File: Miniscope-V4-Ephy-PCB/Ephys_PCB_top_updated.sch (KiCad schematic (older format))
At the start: 41 parts, among them J1 34 Circuit Slimslack Connector, J10 Conn_01x01, J11 Conn_01x01, J12 Conn_01x01, J13 Conn_01x01, J4 Conn_01x01, J5 Conn_01x01, J8 Conn_01x01, U1 ATSAMS70N21A-CFNT, U2 RHD2132_QFN-RHD2132, U3 ABM8G-12.000MHZ-4Y-T3, U4 TXB0304RUT, U5 LTST-C191KRKT, U6 TLV7103318DSER

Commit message: Update schematic and footprints
* Replaced MCU symbol, pinout, and footprint with correct one (TFBGA version).
* Created and replaced slimstack connector with the correct one.
* Replaced crystal oscillator with better symbol
* Tried to link as many footprints as possible to those contained in the Aharoni KiCad Library.
* TODO: Add transistor to drive status LED.
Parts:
- removed C1, C3: GRM155R60J475ME87D, cap_GRM155R60J475ME47D:GRM155R60J475ME47D, symbol .Capacitor:GRM155R60J475ME87D
- removed U1: ATSAMS70N21A-CFNT, ATSAMS70N21ACFNT:ATSAMS70N21A-CFNT, symbol Ephys_PCB_top_updated-rescue:ATSAMS70N21A-CFNT-ATSAMS7-N21
- removed U3: ABM8G-12.000MHZ-4Y-T3, ABM8G-12:OSCSC320X250X100N, symbol Ephys_PCB_top_updated-rescue:ABM8G-12.000MHZ-4Y-T3-ABM8G-12.000MHZ-4Y-T3
- removed U6: TLV7103318DSER, TLV7103318DSER_ldo:TLV7103318DSER, symbol .Regulator_Linear:TLV7103318DSER
- added C1, C3: 4.7uF, .Capacitor:C_0402_1005Metric_L, symbol .Device:C_Small
- added U1: ATSAME70N21A-CN, .Package_BGA:BGA_100_CP80_10X10_900X900X110B40L, symbol .MCU:ATSAME70N21A-CN
- added U3: TLV7103318DSER, .Package_SON:SON_6_P50_150X150X80L50X25L, symbol .Regulator_Linear:TLV7103318DSER
- added Y1: ABM8G-12.000MHZ-4Y-T3, .Oscillator:OSCCC320X250X100L80X100, symbol .Oscillator:ABM8G-12.000MHZ-4Y-T3
- J1: footprint Connector_Molex:Molex_SlimStack_55560-0341_2x17_P0.50mm_Vertical -> .Connector:SS_5046223412
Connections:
- net labels added: VDDUTMIC
- net labels removed: LINEVALID, SPI1_NPCS0, VDDMIC
- wire segments 246 -> 235
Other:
- note removed: "Should have overlapping pins (pins 2 and 4) in the schematic"
- note removed: "You had 1.8V connected to VDDOUT which I don't think is correct."
- moved on the sheet: C17, C18, R1, R3, R4

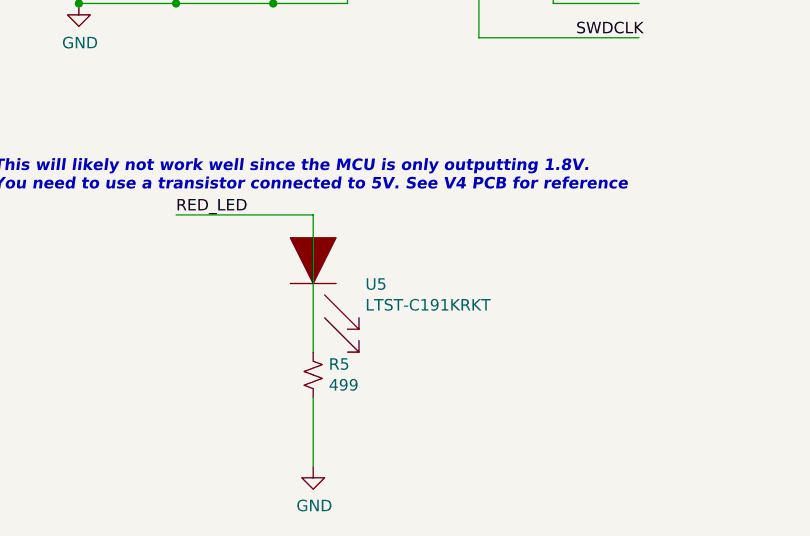
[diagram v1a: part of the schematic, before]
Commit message: Group components in PCB layout
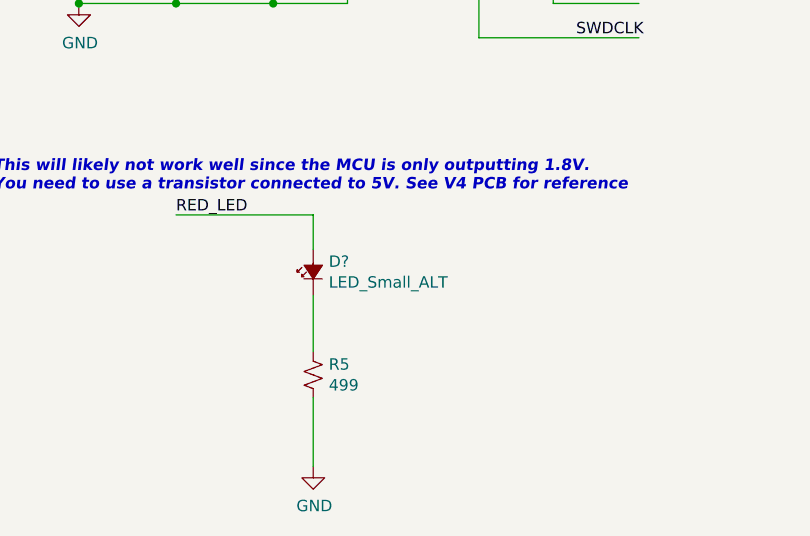
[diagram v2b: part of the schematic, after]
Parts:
- removed U5: LTST-C191KRKT, LED_SMD:LED_0402_1005Metric, symbol .LED:LTST-C191KRKT
- added D?: LED_Small_ALT, LED_SMD:LED_0402_1005Metric, symbol .Device:LED_Small_ALT
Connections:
- wire segments 235 -> 236
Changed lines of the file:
@@
 $EndComp
-$Comp
-L .LED:LTST-C191KRKT U5
-U 1 1 5F09DD3F
-P 10150 9875
-F 0 "U5" V 10204 10103 50  0000 L CNN
-F 1 "LTST-C191KRKT" V 10295 10103 50  0000 L CNN
-F 2 "LED_SMD:LED_0402_1005Metric" H 10150 9875 50  0001 C CNN
-F 3 "" H 10150 9875 50  0001 C CNN
-	1    10150 9875
-	0    1    1    0
-$EndComp
-Wire Wire Line
-	10150 9625 10150 10225
 $Comp
 L power:GND #PWR0128
@@
 	0    1    1    0
 $EndComp
+$Comp
+L .Device:LED_Small_ALT D?
+U 1 1 5F58077D
+P 10150 9875
+F 0 "D?" V 10196 9807 50  0000 R CNN
+F 1 "LED_Small_ALT" V 10105 9807 50  0000 R CNN
+F 2 "LED_SMD:LED_0402_1005Metric" V 10150 9875 50  0001 C CNN
+F 3 "~" V 10150 9875 50  0001 C CNN
+	1    10150 9875
+	0    -1   -1   0
+$EndComp
+Wire Wire Line
+	10150 9625 10150 9775
+Wire Wire Line
+	10150 9975 10150 10225
 $EndSCHEMATC

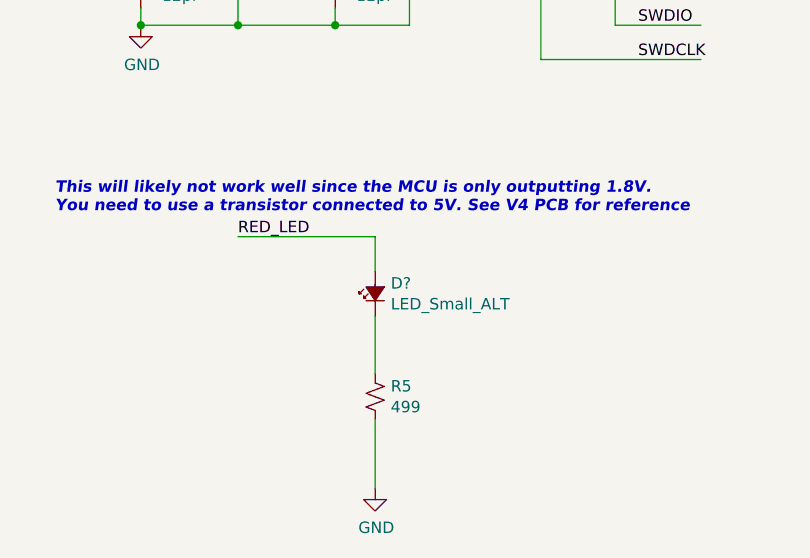
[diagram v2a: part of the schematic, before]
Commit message: Update Board Setup Specifications
Via: 0.15mm/0,3mm
Trace/Space: 3mil/3mil
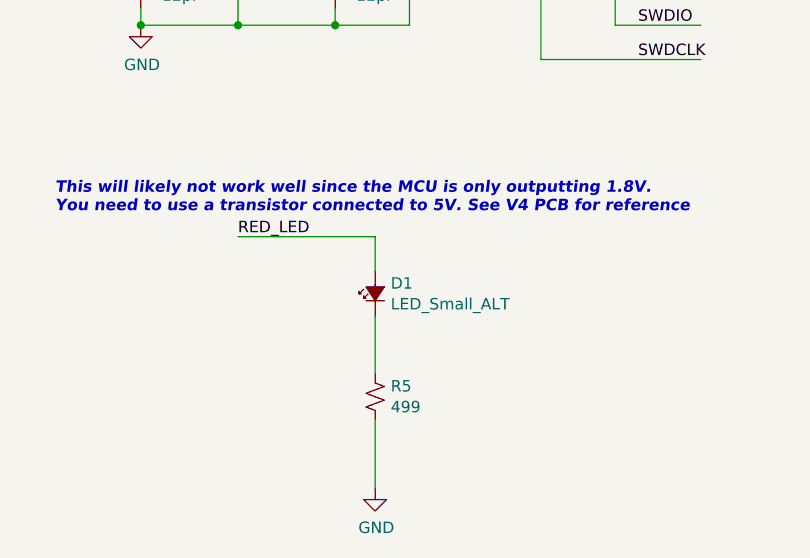
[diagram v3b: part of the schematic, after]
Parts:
- gave numbers to parts that had none: 1
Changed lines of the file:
@@
 $EndComp
 $Comp
-L .Device:LED_Small_ALT D?
+L .Device:LED_Small_ALT D1
 U 1 1 5F58077D
 P 10150 9875
-F 0 "D?" V 10196 9807 50  0000 R CNN
+F 0 "D1" V 10196 9807 50  0000 R CNN
 F 1 "LED_Small_ALT" V 10105 9807 50  0000 R CNN
 F 2 "LED_SMD:LED_0402_1005Metric" V 10150 9875 50  0001 C CNN

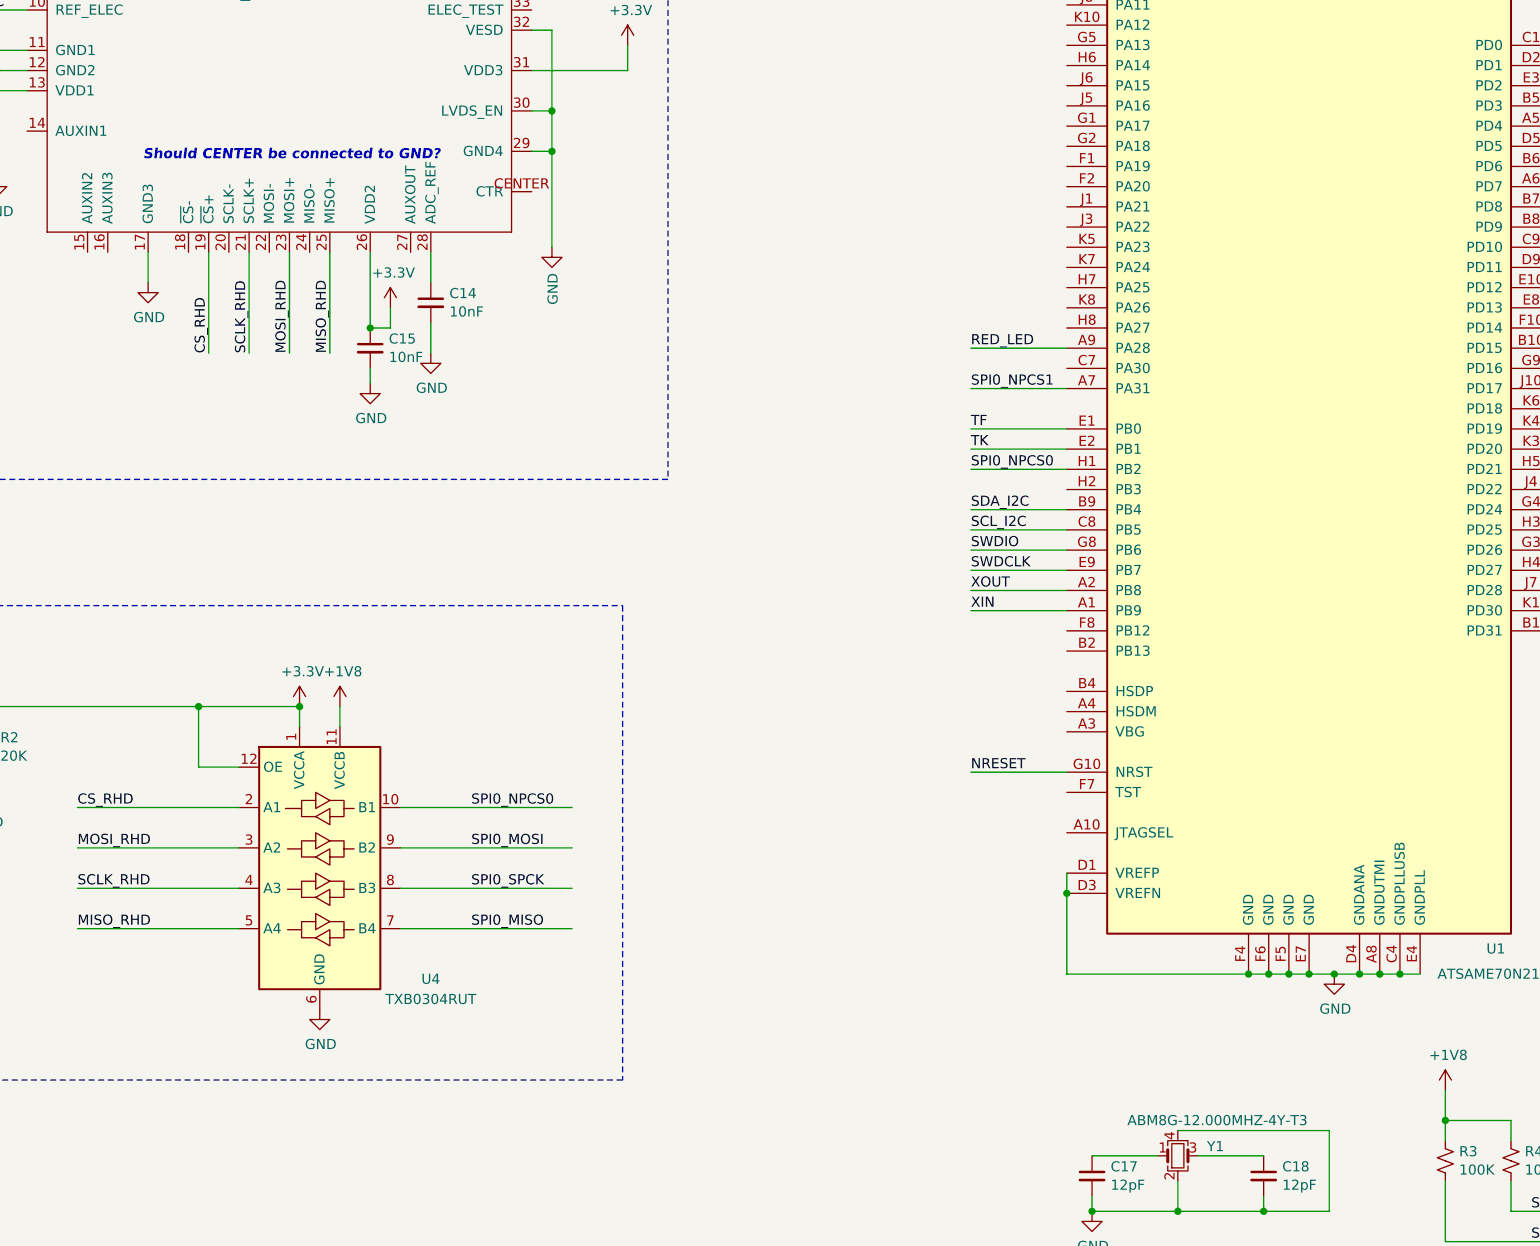
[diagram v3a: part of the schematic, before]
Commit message: Move things around in PCBnew and add prelim board outline.
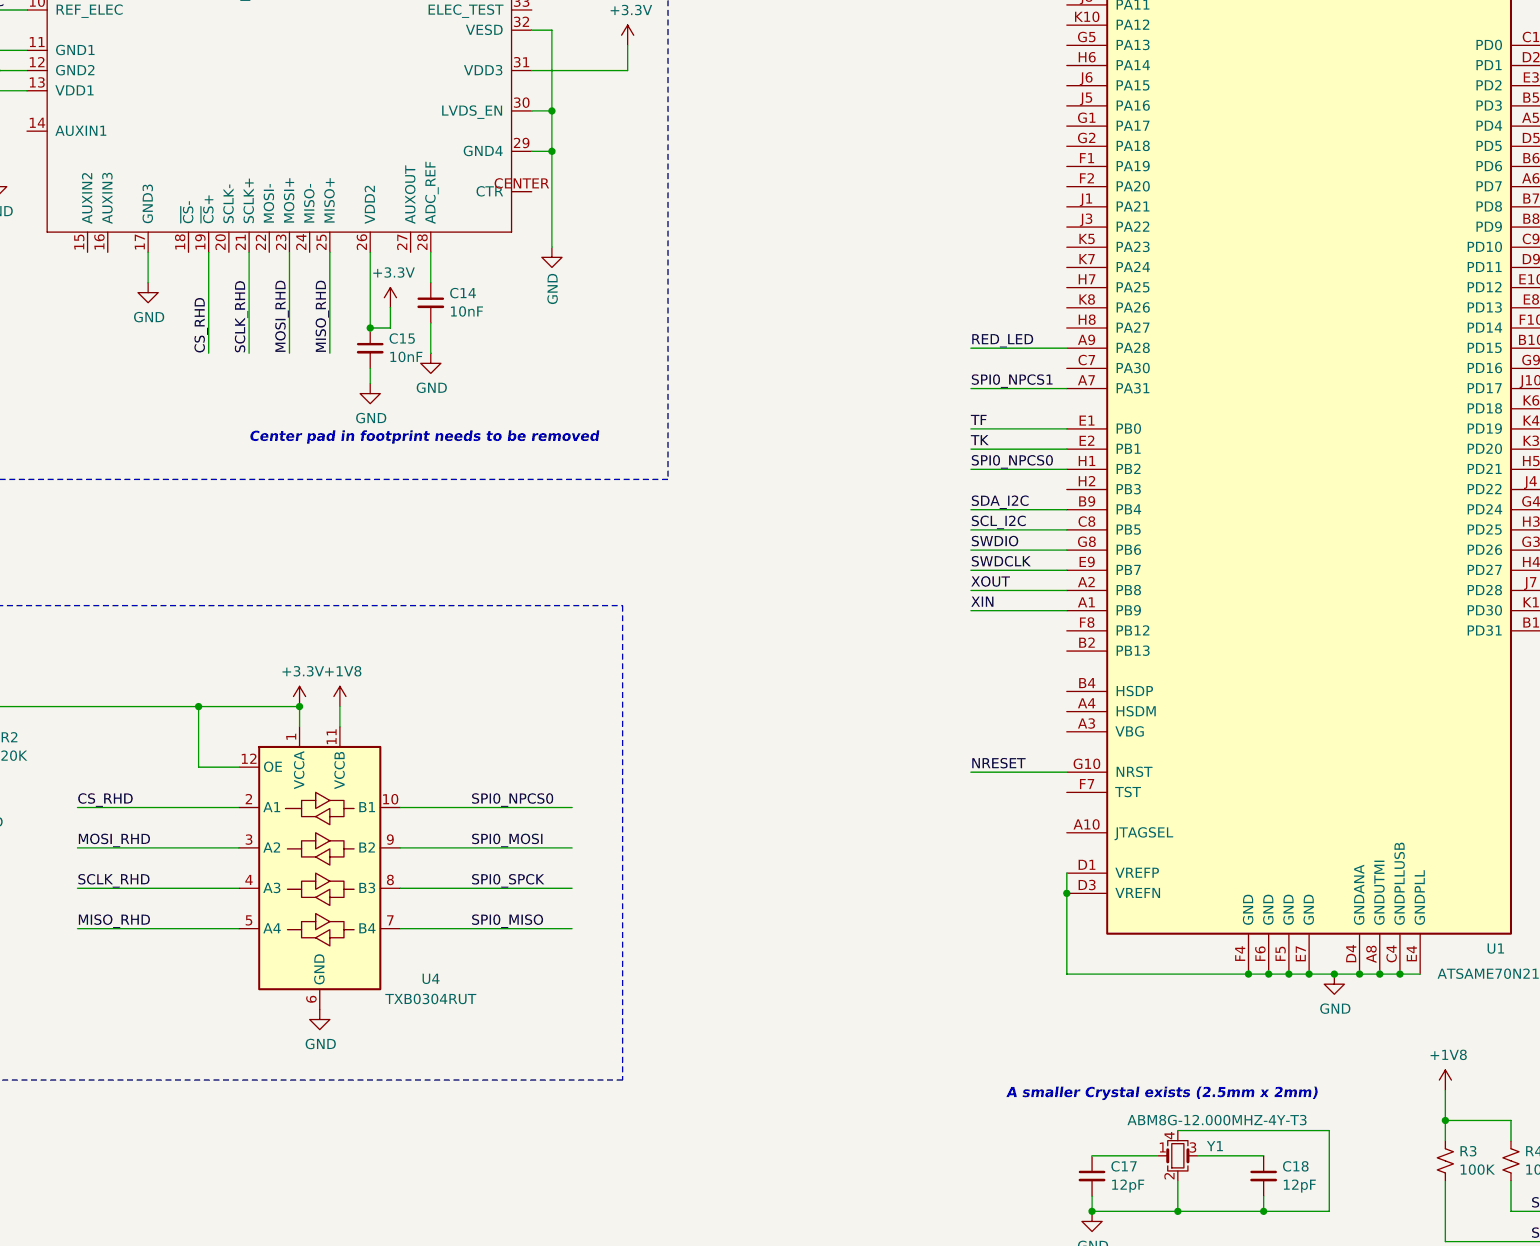
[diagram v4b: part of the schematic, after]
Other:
- note added: "A smaller Crystal exists (2.5mm x 2mm)"
- note added: "Center pad in footprint needs to be removed"
- note removed: "Should CENTER be connected to GND?"
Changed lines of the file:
@@
 Wire Wire Line
 	6350 3050 6825 3050
-Text Notes 4425 3500 0    50   Italic 10
-Should CENTER be connected to GND?
+Text Notes 4950 4900 0    50   Italic 10
+Center pad in footprint needs to be removed
 $Comp
 L power:+3.3V #PWR09
@@
 Wire Wire Line
 	10150 9975 10150 10225
+Text Notes 8700 8150 0    50   Italic 10
+A smaller Crystal exists (2.5mm x 2mm)
 $EndSCHEMATC
